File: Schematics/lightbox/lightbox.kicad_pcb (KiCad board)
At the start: 2 copper layers, 50.5 x 61.5 mm, 25 parts, among them J1 Screw_Terminal_01x04, J2 Conn_01x11_Female, J3 Conn_01x07_Female, J4 Conn_02x03_Odd_Even, Q1 IRF740, Q2 IRF740, U1 74AHCT595, U2 74HC595, U3 ATtiny85-20P, U4 LM317_TO-220

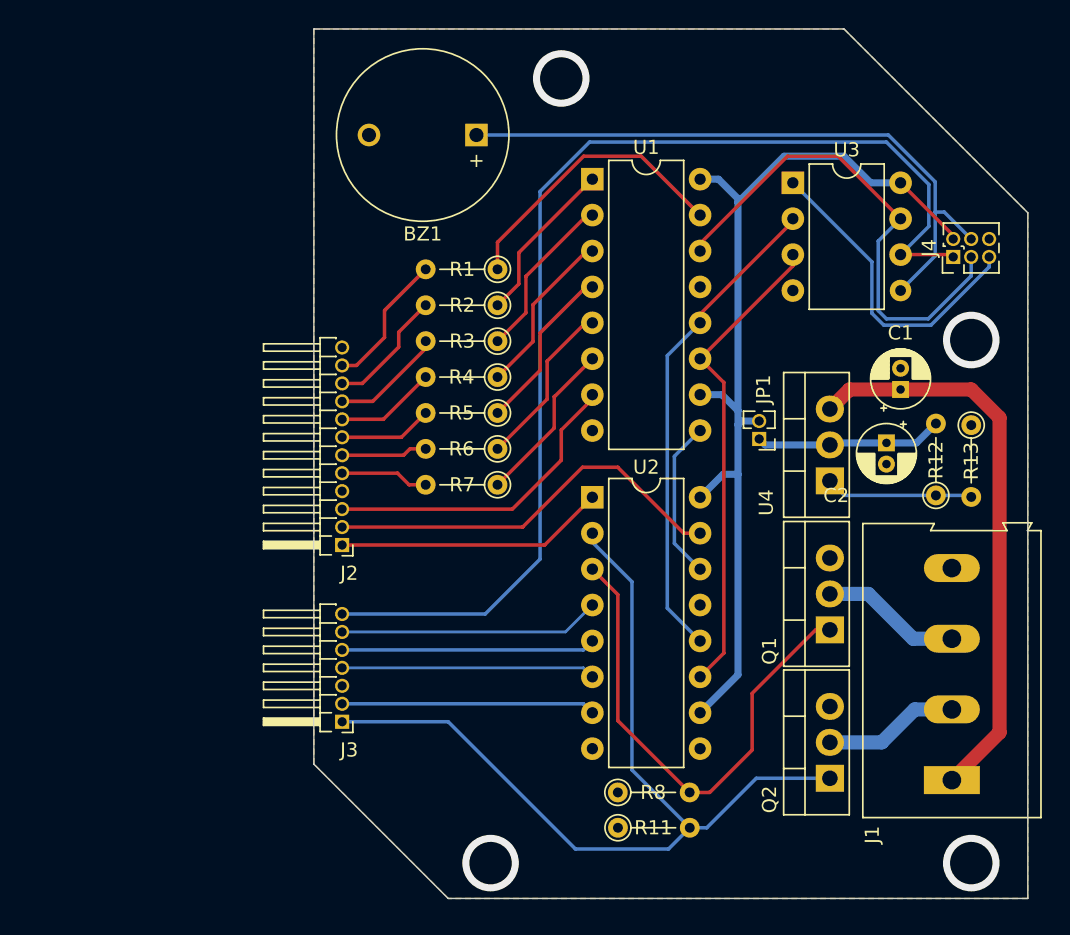
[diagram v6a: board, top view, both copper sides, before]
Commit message: Replace IRF740 by IRF530; Update PCB Layout; Plot PCB Layers
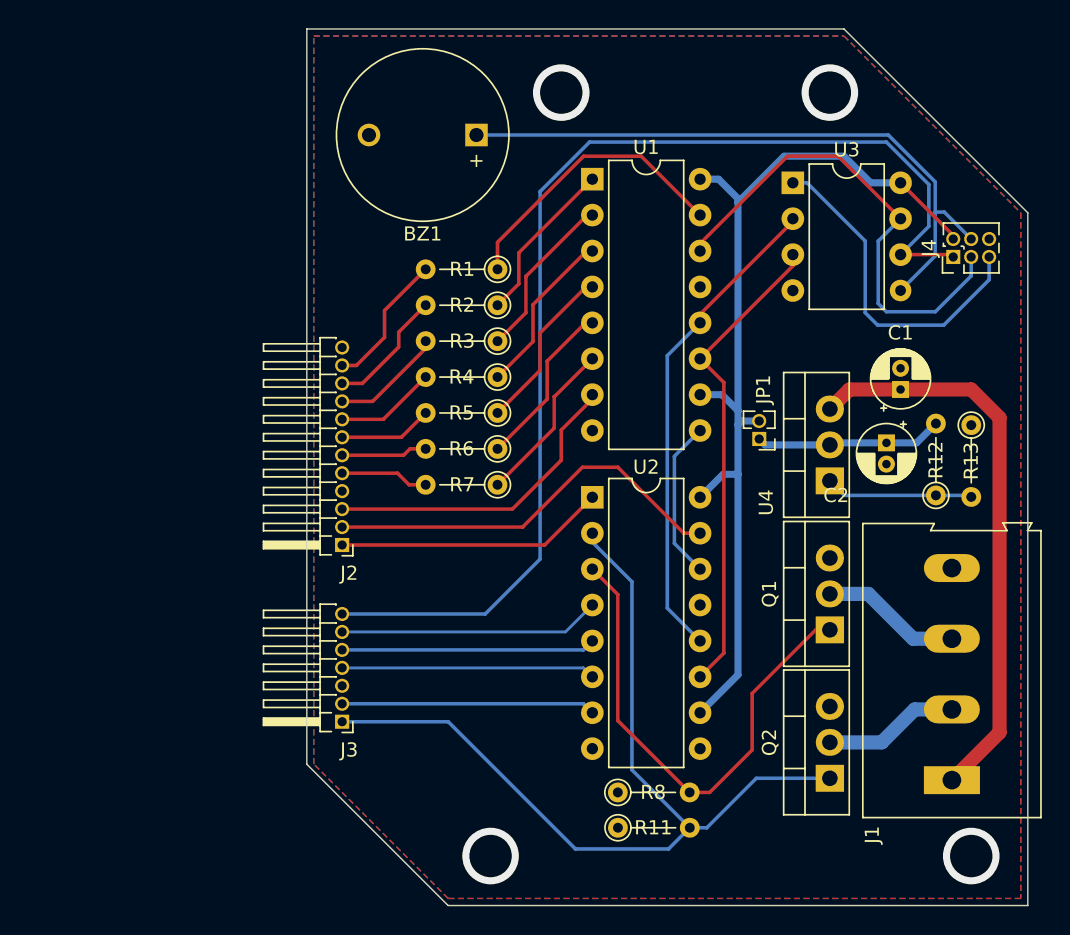
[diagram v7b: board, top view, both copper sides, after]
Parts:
- Q1, Q2: value IRF740 -> IRF530
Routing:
- net /ISP_RST: track 22.6 -> 24.0 mm
- net /D_{2}: track 35.7 -> 35.0 mm
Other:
- board size 50.5 x 61.5 mm -> 51 x 62 mm

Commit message: Update PCB layout; Clear acid traps; Generate new layers
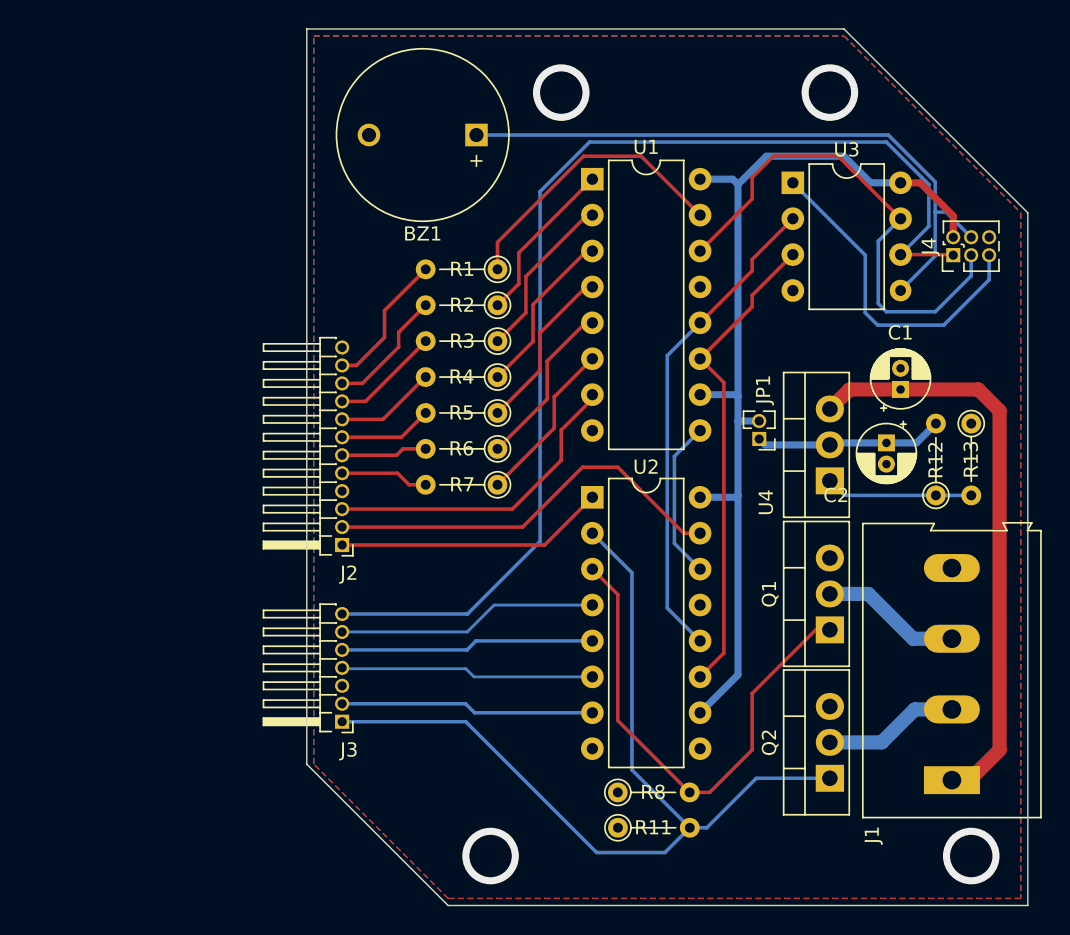
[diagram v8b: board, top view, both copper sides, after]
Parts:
- moved J4 0.12 mm to (168.2, 85.0)
- moved R13 0.11 mm to (169.5, 96.9)
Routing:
- net +12V: track 40.4 -> 41.4 mm
- net /D_{1}: track 81.4 -> 80.6 mm
- net /D_{2}: track 35.0 -> 35.7 mm
